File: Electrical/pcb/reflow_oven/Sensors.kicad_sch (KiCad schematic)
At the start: 0 parts

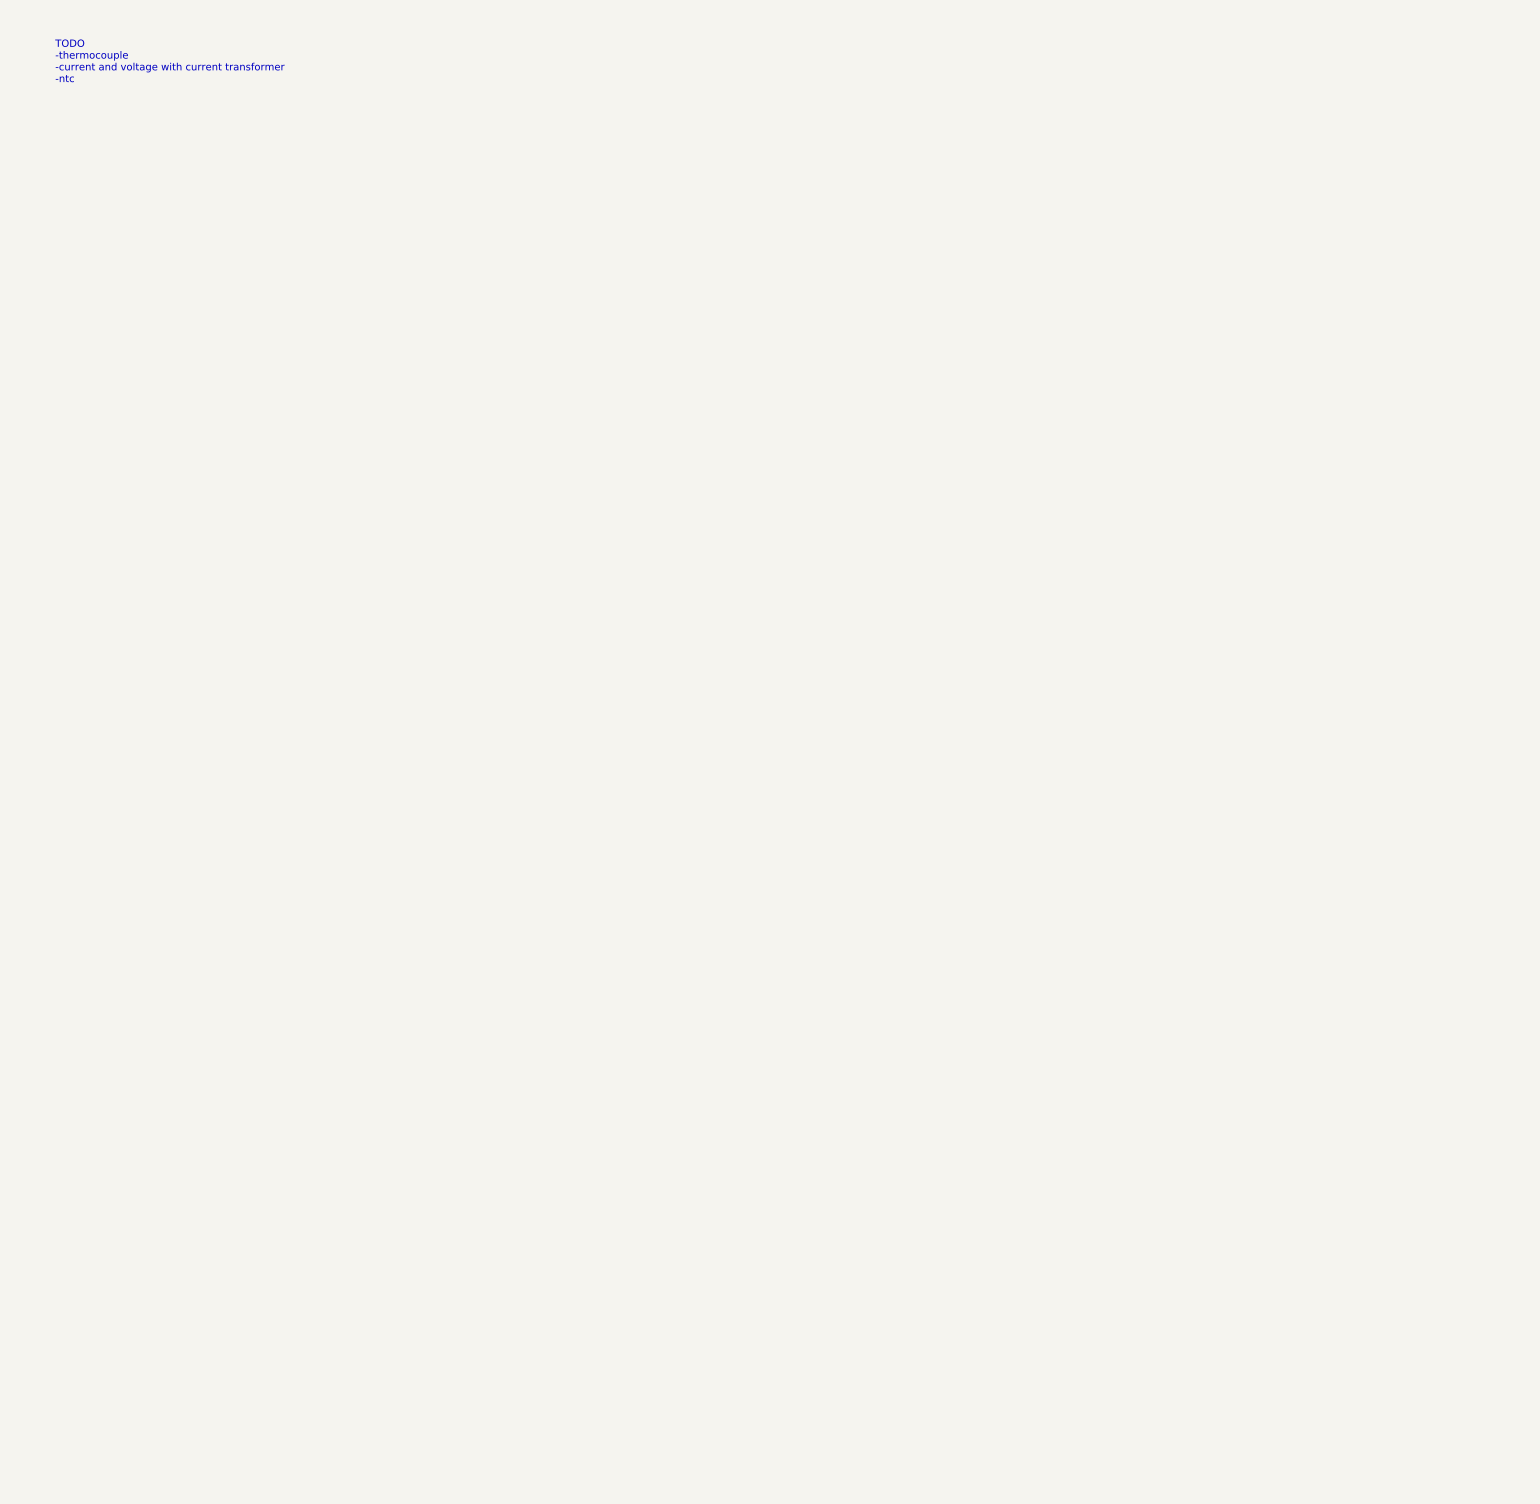
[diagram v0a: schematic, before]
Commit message: analog Sensing
-voltage and current sensor
-zero crossing
-temperature
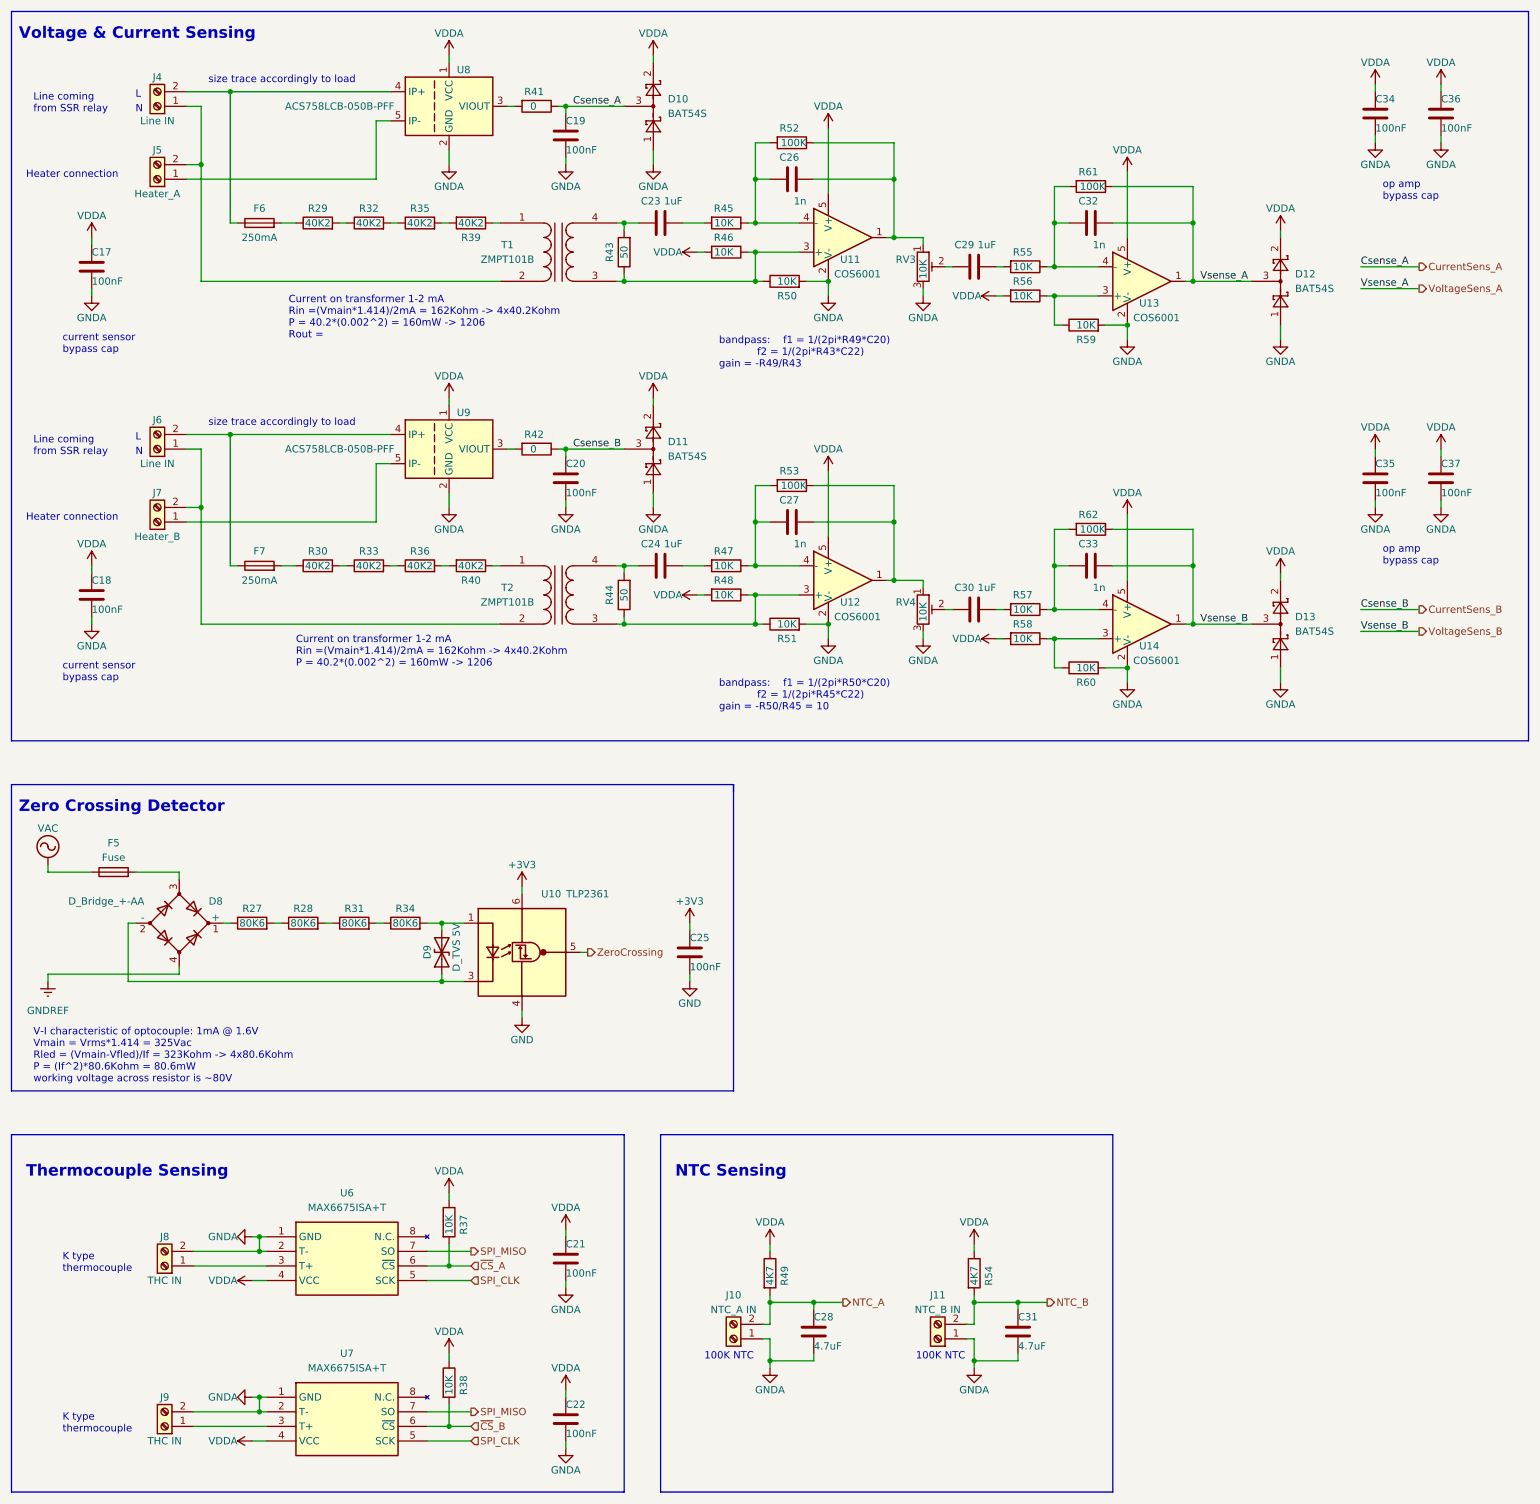
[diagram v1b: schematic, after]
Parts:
- added C17, C18, C19, C20, C21, C22, C25, C34, C35, C36, C37: 100nF, Capacitor_SMD:C_0603_1608Metric, symbol Device:C
- added C23, C24, C29, C30: 1uF, Capacitor_SMD:C_0805_2012Metric, symbol Device:C
- added C26, C27, C32, C33: 1n, Capacitor_SMD:C_0603_1608Metric, symbol Device:C
- added C28, C31: 4.7uF, Capacitor_SMD:C_0805_2012Metric, symbol Device:C
- added D10, D11, D12, D13: BAT54S, Package_TO_SOT_SMD:SOT-23, symbol Diode:BAT54S
- added D8: D_Bridge_+-AA, footprint_lib:DIP825W58P510L832H472Q4N, symbol Device:D_Bridge_+-AA
- added D9: D_TVS 5V, Diode_SMD:D_SOD-523, symbol Device:D_TVS
- added F5: Fuse, footprint_lib:Circular_fuse, symbol Device:Fuse
- added F6, F7: 250mA, footprint_lib:Circular_fuse, symbol Device:Fuse
- added J10: NTC_A IN, TerminalBlock_Phoenix:TerminalBlock_Phoenix_MPT-0,5-2-2.54_1x02_P2.54mm_Horizontal, symbol Connector:Screw_Terminal_01x02
- added J11: NTC_B IN, TerminalBlock_Phoenix:TerminalBlock_Phoenix_MPT-0,5-2-2.54_1x02_P2.54mm_Horizontal, symbol Connector:Screw_Terminal_01x02
- added J4, J6: Line IN, TerminalBlock:TerminalBlock_bornier-2_P5.08mm, symbol Connector:Screw_Terminal_01x02
- added J5: Heater_A, TerminalBlock:TerminalBlock_bornier-2_P5.08mm, symbol Connector:Screw_Terminal_01x02
- added J7: Heater_B, TerminalBlock:TerminalBlock_bornier-2_P5.08mm, symbol Connector:Screw_Terminal_01x02
- added J8, J9: THC IN, TerminalBlock_Phoenix:TerminalBlock_Phoenix_MPT-0,5-2-2.54_1x02_P2.54mm_Horizontal, symbol Connector:Screw_Terminal_01x02
- added R27, R28, R31, R34: 80K6, Resistor_SMD:R_0805_2012Metric_Pad1.20x1.40mm_HandSolder, symbol Device:R
- added R29, R30, R32, R33, R35, R36, R39, R40: 40K2, Resistor_SMD:R_1206_3216Metric_Pad1.30x1.75mm_HandSolder, symbol Device:R
- added R37, R38, R45, R46, R47, R48, R50, R51, R55, R56, R57, R58, R59, R60: 10K, Resistor_SMD:R_0603_1608Metric, symbol Device:R
- added R41, R42: 0, Resistor_SMD:R_0603_1608Metric, symbol Device:R
- added R43, R44: 50, Resistor_SMD:R_0805_2012Metric_Pad1.20x1.40mm_HandSolder, symbol Device:R
- added R49, R54: 4K7, Resistor_SMD:R_0603_1608Metric, symbol Device:R
- added R52, R53, R61, R62: 100K, Resistor_SMD:R_0603_1608Metric, symbol Device:R
- added RV3, RV4: 10K, footprint_lib:TC33X2503E, symbol Device:R_Potentiometer_Trim
- added T1, T2: ZMPT101B, footprint_lib:ZMPT101B, symbol Device:Transformer_1P_1S
- added U10: TLP2361, footprint_lib:11-4L1S_5-PIN-SOIC_, symbol Isolator:TLP2748
- added U11, U12, U13, U14: COS6001, Package_TO_SOT_SMD:SOT-23-5, symbol Amplifier_Operational:LM321
- added U6, U7: MAX6675ISA+T, footprint_lib:SOIC127P600X175-8N, symbol comp_lib:MAX6675ISA+T
- added U8, U9: ACS758LCB-050B-PFF, Sensor_Current:Allegro_CB_PFF, symbol Sensor_Current:ACS758xCB-050B-PFF
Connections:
- new net: F7.1, J6.2 (Pin_2), U9.4 (IP+)
- new net: F7.2, R30.1
- new net: C27.2, R53.1, RV4.1, U12.1
- new net: C27.1, R47.1, R53.2, U12.4 (-)
- new net: C33.1, R57.1, R62.2, U14.4 (-)
- new net: R43.1, R46.1, R50.1, T1.3 (SA), U11.3 (+)
- new net: R56.1, R59.1, U13.3 (+)
- new net: C32.1, R55.1, R61.2, U13.4 (-)
- new net: D9.2 (A2), R34.2, U10.1 (A)
- new net: D8.2 (-), D9.1 (A1), U10.3 (K)
- new net: R39.1, T1.1 (AA)
- new net: R35.2, R39.2
- new net: C23.1, R43.2, T1.4 (SB)
- new net: C23.2, R45.2
- new net: R32.2, R35.1
- new net: J8.1 (Pin_1), U6.3 (T+)
- new net: J9.1 (Pin_1), U7.3 (T+)
- new net: R27.2, R28.1
- new net: R28.2, R31.1
- new net: R29.2, R32.1
- new net: R44.1, R48.1, R51.1, T2.3 (SA), U12.3 (+)
- new net: C24.1, R44.2, T2.4 (SB)
- new net: C24.2, R47.2
- new net: J7.1 (Pin_1), U9.5 (IP-)
- new net: J6.1 (Pin_1), J7.2 (Pin_2), T2.2 (AB)
- new net: C26.2, R52.1, RV3.1, U11.1
- new net: C26.1, R45.1, R52.2, U11.4 (-)
- new net: R33.2, R36.1
- new net: R36.2, R40.2
- new net: R58.1, R60.1, U14.3 (+)
- new net: R41.2, U8.3 (VIOUT)
- new net: F6.1, J4.2 (Pin_2), U8.4 (IP+)
- new net: J5.1 (Pin_1), U8.5 (IP-)
- new net: J4.1 (Pin_1), J5.2 (Pin_2), T1.2 (AB)
- new net: F6.2, R29.1
- new net: C29.1, RV3.2
- new net: C29.2, R55.2
- new net: R31.2, R34.1
- new net: R40.1, T2.1 (AA)
- new net: D8.3, F5.2
- new net: R30.2, R33.1
- new net: R42.2, U9.3 (VIOUT)
- new net: C30.2, R57.2
- new net: C30.1, RV4.2
- new net: D8.1 (+), R27.1
- new net +3V3: C25.1, U10.6 (VDD)
- new net CurrentSens_A: C19.1, D10.3, R41.1
- new net CurrentSens_B: C20.1, D11.3, R42.1
- new net GND: C25.2, U10.4 (GND)
- new net GNDA: C17.2, C18.2, C19.2, C20.2, C21.2, C22.2, C28.2, C31.2, C34.2, C35.2, C36.2, C37.2, D10.1, D11.1, D12.1, D13.1, J10.1 (Pin_1), J11.1 (Pin_1), J8.2 (Pin_2), J9.2 (Pin_2), R50.2, R51.2, R59.2, R60.2, RV3.3, RV4.3, U11.2 (V-), U12.2 (V-), U13.2 (V-), U14.2 (V-), U6.1 (GND), U6.2 (T-), U7.1 (GND), U7.2 (T-), U8.2 (GND), U9.2 (GND)
- new net GNDREF: D8.4
- new net NTC_A: C28.1, J10.2 (Pin_2), R49.2
- new net NTC_B: C31.1, J11.2 (Pin_2), R54.2
- new net SPI_CLK: U6.5 (SCK), U7.5 (SCK)
- new net SPI_MISO: U6.7 (SO), U7.7 (SO)
- new net VAC: F5.1
- new net VDDA: C17.1, C18.1, C21.1, C22.1, C34.1, C35.1, C36.1, C37.1, D10.2, D11.2, D12.2, D13.2, R37.1, R38.1, R46.2, R48.2, R49.1, R54.1, R56.2, R58.2, U11.5 (V+), U12.5 (V+), U13.5 (V+), U14.5 (V+), U6.4 (VCC), U7.4 (VCC), U8.1 (VCC), U9.1 (VCC)
- new net VoltageSens_A: C32.2, D12.3, R61.1, U13.1
- new net VoltageSens_B: C33.2, D13.3, R62.1, U14.1
- new net ZeroCrossing: U10.5 (VO)
- new net ~{CS}_A: R37.2, U6.6 (~{CS})
- new net ~{CS}_B: R38.2, U7.6 (~{CS})
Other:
- note added: "100K NTC"
- note added: "Current on transformer 1-2 mA Rin =(Vmain*1.414)/2mA = 162Kohm -> 4x40.2Kohm P = 40.2*(0.002^2) = 160mW -> 1206"
- note added: "Current on transformer 1-2 mA Rin =(Vmain*1.414)/2mA = 162Kohm -> 4x40.2Kohm P = 40.2*(0.002^2) = 160mW -> 1206 Rout ="
- note added: "Heater connection"
- note added: "K type thermocouple"
- note added: "L"
- note added: "Line coming from SSR relay"
- note added: "N"
- note added: "NTC Sensing"
- note added: "Thermocouple Sensing"
- note added: "V-I characteristic of optocouple: 1mA @ 1.6V Vmain = Vrms*1.414 = 325Vac Rled = (Vmain-Vfled)/If = 323Kohm -> 4x80.6Kohm P = (If^2)*80.6Kohm = 80.6mW working voltage across resistor is ~80V"
- note added: "Voltage & Current Sensing"
- note added: "Zero Crossing Detector"
- note added: "bandpass: f1 = 1/(2pi*R49*C20) f2 = 1/(2pi*R43*C22) gain = -R49/R43"
- note added: "bandpass: f1 = 1/(2pi*R50*C20) f2 = 1/(2pi*R45*C22) gain = -R50/R45 = 10"
- note added: "current sensor bypass cap"
- note added: "op amp bypass cap"
- note added: "size trace accordingly to load"
- note removed: "TODO -thermocouple -current and voltage with current transformer -ntc"

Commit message: schematic
-interface
-micro
todo
output
routing
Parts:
- renumbered J8 to J10, J9 to J11, J10 to J12, J11 to J13, J4 to J6, J5 to J7, J6 to J8, J7 to J9, R27 to R31, R28 to R32, R29 to R33, R30 to R34, R31 to R35, R32 to R36, R33 to R37, R34 to R38, R35 to R39, R36 to R40, R37 to R41, R38 to R42, R39 to R43, R40 to R44, R41 to R45, R42 to R46, R43 to R47, R44 to R48, R45 to R49, R46 to R50, R47 to R51, R48 to R52, R49 to R53, R50 to R54, R51 to R55, R52 to R56, R53 to R57, R54 to R58, R55 to R59, R56 to R60, R57 to R61, R58 to R62, R59 to R63, R60 to R64, R61 to R65, R62 to R66

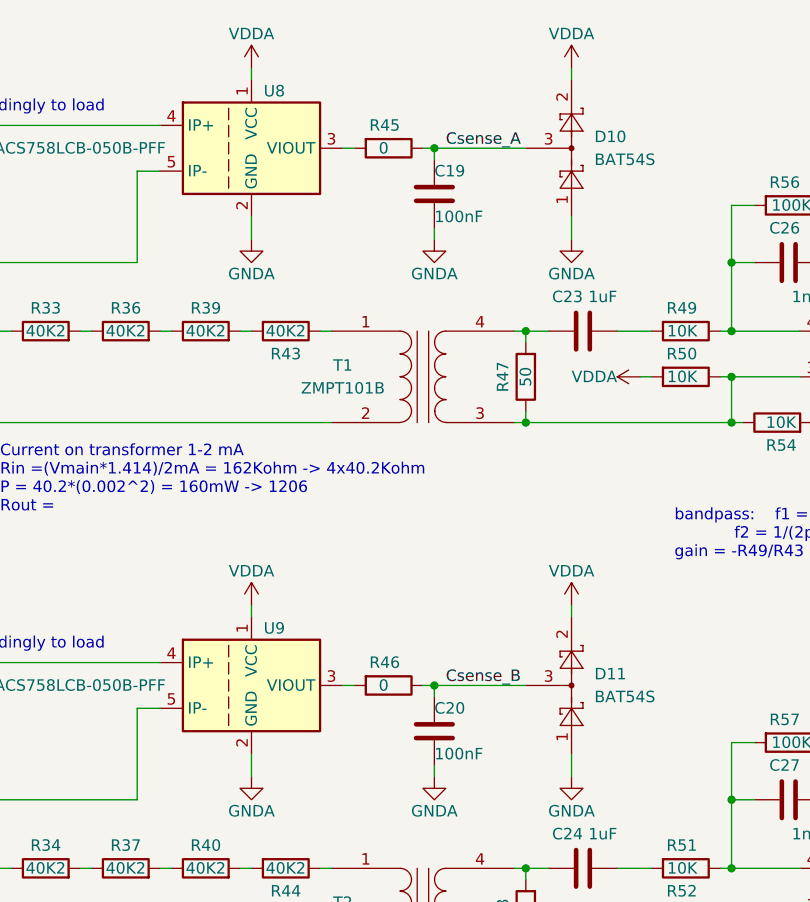
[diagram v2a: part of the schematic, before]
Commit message: addon
- ferrites application notes
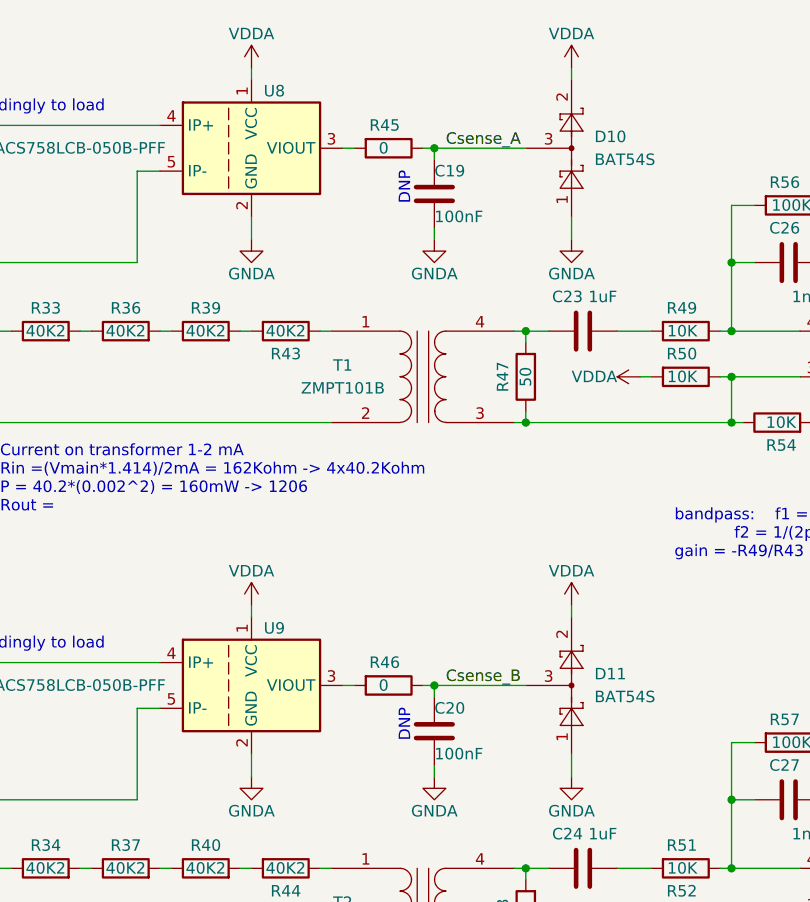
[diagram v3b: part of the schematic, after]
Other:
- note added: "DNP"
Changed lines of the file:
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@@
+    (effects (font (size 1.27 1.27)) (justify left bottom))
+  )
+  (text "DNP\n" (at 111.76 41.91 90)
     (effects (font (size 1.27 1.27)) (justify left bottom))
   )
@@
     (effects (font (size 2 2) (thickness 0.4) bold) (justify left bottom))
   )
+  (text "DNP\n" (at 111.76 101.6 90)
+    (effects (font (size 1.27 1.27)) (justify left bottom))
+  )
   (text "100K NTC" (at 138.43 254 0)
